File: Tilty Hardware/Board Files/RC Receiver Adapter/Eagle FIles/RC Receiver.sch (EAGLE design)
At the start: 19 parts, among them U1 ATMEGA328P, U2 LM2931, Y1 16MHz

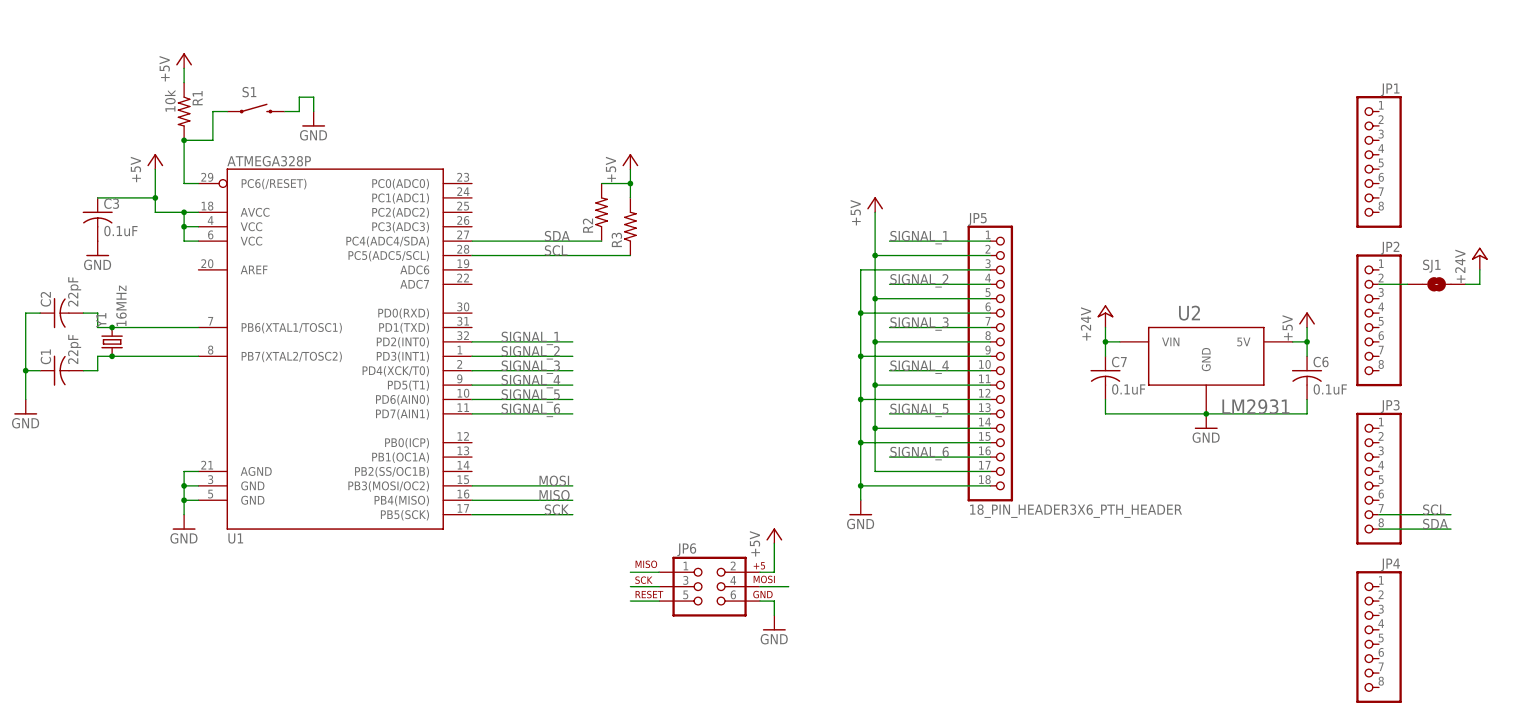
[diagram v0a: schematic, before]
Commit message: Finally got TiltyIMU class working! updated some other programs, worked on RC receiver add-on
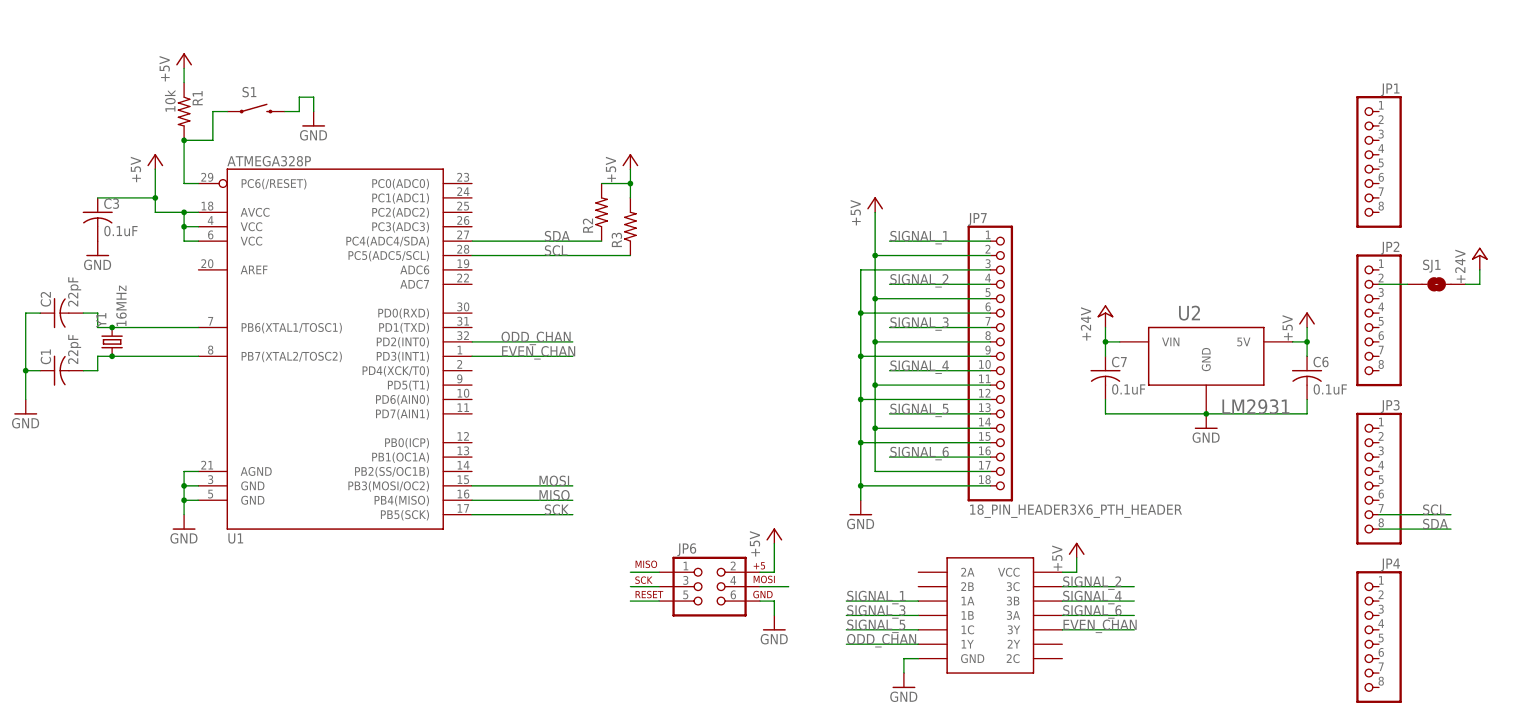
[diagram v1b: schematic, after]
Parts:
- added U$1: C74HC407514-SOIC, My Parts:C74HC407514-SOIC
- Y1: device SparkFun-FreqCtrl:CRYSTALSMD -> SparkFun-FreqCtrl:CRYSTAL5X3
- renumbered JP5 to JP7
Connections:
- new net EVEN_CHAN: U$1.3Y, U1.PD3(INT1)
- new net ODD_CHAN: U$1.1Y, U1.PD2(INT0)
- net +5V: now also U$1.VCC
- net GND: now also U$1.GND
- net SIGNAL_1: now also U$1.1A; no longer U1.PD2(INT0)
- net SIGNAL_2: now also U$1.3C; no longer U1.PD3(INT1)
- net SIGNAL_3: now also U$1.1B; no longer U1.PD4(XCK/T0)
- net SIGNAL_4: now also U$1.3B; no longer U1.PD5(T1)
- net SIGNAL_5: now also U$1.1C; no longer U1.PD6(AIN0)
- net SIGNAL_6: now also U$1.3A; no longer U1.PD7(AIN1)

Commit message: Nearly finished R/C receiver add-on, updated things to-do
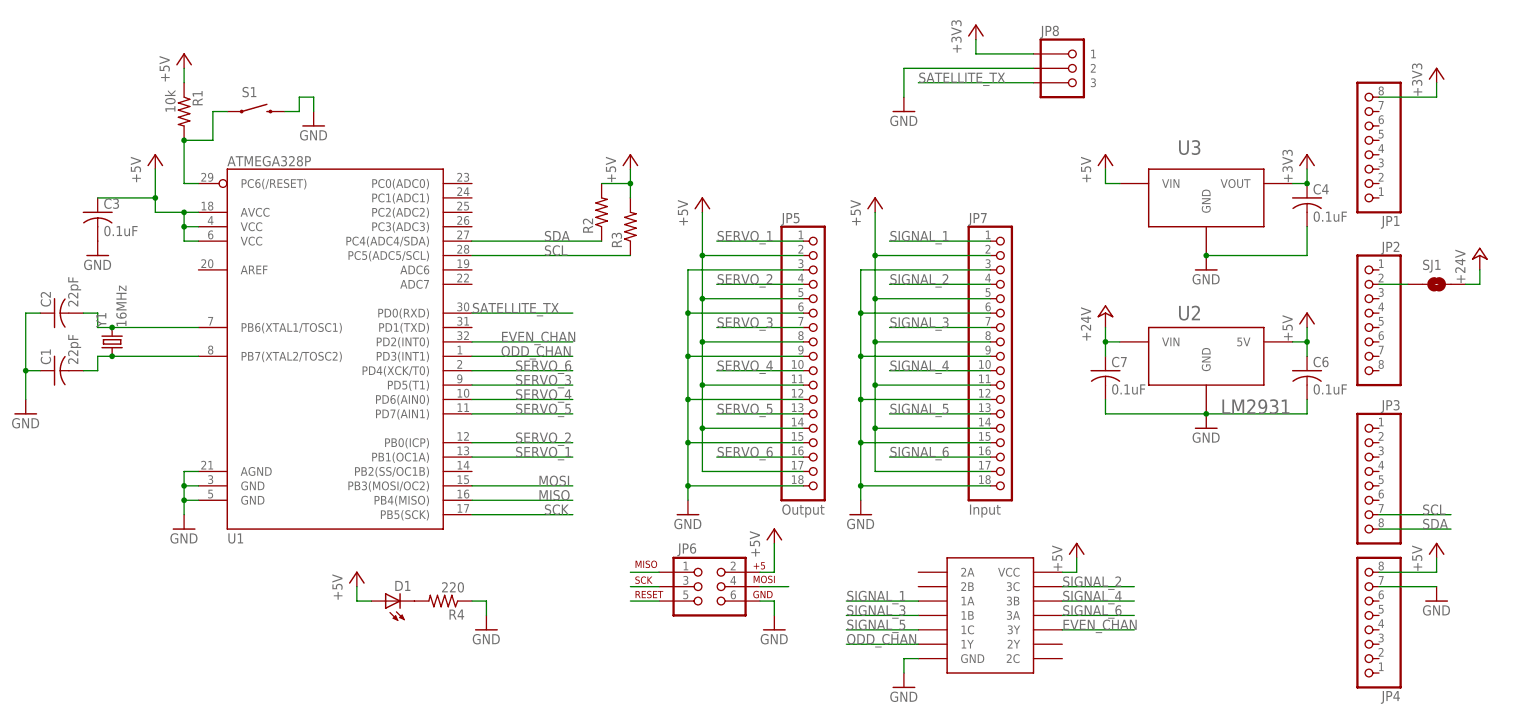
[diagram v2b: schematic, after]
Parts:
- added C4: 0.1uF, resistor:C-USC0603
- added D1: (no value), SparkFun-LED:LED-GREENLED-0805_NO_SILK
- added JP5: Output, My Parts:18_PIN_HEADER3X6_PTH_HEADER
- added JP8: 3-PIN_JST_ZH_PTH_CONNECTORRIGHT_ANGLE_PTH, My Parts:3-PIN_JST_ZH_PTH_CONNECTORRIGHT_ANGLE_PTH
- added R4: 220, resistor:R-US_R0603
- added U3: AP7313SOT23R, My Parts:AP7313SOT23R
- JP7: value 18_PIN_HEADER3X6_PTH_HEADER -> Input
- renumbered U$1 to U4
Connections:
- new net +3V3: C4.1, JP1.8, JP8.1, U3.VOUT
- new net N$8: D1.C, R4.2
- new net SATELLITE_TX: JP8.3, U1.PD0(RXD)
- new net SERVO_1: JP5.1, U1.PB1(OC1A)
- new net SERVO_2: JP5.4, U1.PB0(ICP)
- new net SERVO_3: JP5.7, U1.PD5(T1)
- new net SERVO_4: JP5.10, U1.PD6(AIN0)
- new net SERVO_5: JP5.13, U1.PD7(AIN1)
- new net SERVO_6: JP5.16, U1.PD4(XCK/T0)
- net +5V: now also D1.A, JP4.8, JP5.11, JP5.14, JP5.17, JP5.2, JP5.5, JP5.8, U3.VIN
- net EVEN_CHAN: now also U1.PD2(INT0); no longer U1.PD3(INT1)
- net GND: now also C4.2, JP4.7, JP5.12, JP5.15, JP5.18, JP5.3, JP5.6, JP5.9, JP8.2, R4.1, U3.GND
- net ODD_CHAN: now also U1.PD3(INT1); no longer U1.PD2(INT0)
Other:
- moved on the sheet: JP1, JP4

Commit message: Nearly finished RC Receiver add-on prototype, worked on TiltyIMU library
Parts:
- added JP10: (no value), SparkFun-Connectors:M03X2NO_SILK
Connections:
- new net A0: JP10.1, U1.PC0(ADC0)
- new net A1: JP10.3, U1.PC1(ADC1)
- new net A2: JP10.5, U1.PC2(ADC2)
- new net A3: JP10.6, U1.PC3(ADC3)
- new net ARDUINO_TX: JP10.2, U1.PD1(TXD)
- net GND: now also JP2.1, JP3.1
- net SATELLITE_TX: now also JP10.4
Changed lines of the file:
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@@
 <part name="GND4" library="supply1" deviceset="GND" device=""/>
 <part name="P+4" library="supply1" deviceset="+5V" device=""/>
-<part name="S1" library="SparkFun-Electromechanical" deviceset="SWITCH-MOMENTARY-2" device="SMD"/>
 <part name="GND5" library="supply1" deviceset="GND" device=""/>
 <part name="JP6" library="SparkFun-Connectors" deviceset="AVR_SPI_PRG_6" device="2X3_LOCK"/>
@@
 <part name="R4" library="resistor" deviceset="R-US_" device="R0603" value="220"/>
 <part name="GND13" library="supply1" deviceset="GND" device=""/>
+<part name="GND14" library="supply1" deviceset="GND" device=""/>
+<part name="GND15" library="supply1" deviceset="GND" device=""/>
+<part name="JP10" library="SparkFun-Connectors" deviceset="M03X2" device="NO_SILK"/>
+<part name="S1" library="SparkFun-Electromechanical" deviceset="SWITCH-MOMENTARY-2" device="SMD"/>
 </parts>
 <sheets>
@@
 <instance part="GND4" gate="1" x="35.56" y="40.64"/>
 <instance part="P+4" gate="1" x="30.48" y="106.68"/>
-<instance part="S1" gate="G$1" x="48.26" y="114.3" smashed="yes">
-<attribute name="NAME" x="45.72" y="116.84" size="1.778" layer="95"/>
-</instance>
 <instance part="GND5" gate="1" x="58.42" y="111.76"/>
 <instance part="JP6" gate="G$1" x="127" y="30.48" smashed="yes">
@@
 <instance part="R4" gate="G$1" x="81.28" y="27.94" rot="R180"/>
 <instance part="GND13" gate="1" x="88.9" y="22.86"/>
+<instance part="GND14" gate="1" x="269.24" y="86.36"/>
+<instance part="GND15" gate="1" x="254" y="53.34"/>
+<instance part="JP10" gate="G$1" x="99.06" y="121.92"/>
+<instance part="S1" gate="G$1" x="48.26" y="114.3" smashed="yes">
+<attribute name="NAME" x="45.72" y="116.84" size="1.778" layer="95"/>
+</instance>
 </instances>
 <busses>
@@
 </segment>
 <segment>
-<pinref part="S1" gate="G$1" pin="2"/>
-<wire x1="53.34" y1="114.3" x2="55.88" y2="114.3" width="0.1524" layer="91"/>
 <wire x1="55.88" y1="114.3" x2="55.88" y2="116.84" width="0.1524" layer="91"/>
 <wire x1="55.88" y1="116.84" x2="58.42" y2="116.84" width="0.1524" layer="91"/>
 <pinref part="GND5" gate="1" pin="GND"/>
 <wire x1="58.42" y1="116.84" x2="58.42" y2="114.3" width="0.1524" layer="91"/>
+<pinref part="S1" gate="G$1" pin="2"/>
+<wire x1="55.88" y1="114.3" x2="53.34" y2="114.3" width="0.1524" layer="91"/>
 </segment>
 <segment>
@@
 <wire x1="88.9" y1="27.94" x2="88.9" y2="25.4" width="0.1524" layer="91"/>
 </segment>
+<segment>
+<pinref part="JP2" gate="A" pin="1"/>
+<wire x1="246.38" y1="86.36" x2="251.46" y2="86.36" width="0.1524" layer="91"/>
+<wire x1="251.46" y1="86.36" x2="251.46" y2="93.98" width="0.1524" layer="91"/>
+<wire x1="251.46" y1="93.98" x2="269.24" y2="93.98" width="0.1524" layer="91"/>
+<wire x1="269.24" y1="93.98" x2="269.24" y2="88.9" width="0.1524" layer="91"/>
+<pinref part="GND14" gate="1" pin="GND"/>
+</segment>
+<segment>
+<pinref part="JP3" gate="A" pin="1"/>
+<wire x1="246.38" y1="58.42" x2="254" y2="58.42" width="0.1524" layer="91"/>
+<wire x1="254" y1="58.42" x2="254" y2="55.88" width="0.1524" layer="91"/>
+<pinref part="GND15" gate="1" pin="GND"/>
+</segment>
 </net>
 <net name="+24V" class="0">
@@
 <wire x1="35.56" y1="109.22" x2="35.56" y2="101.6" width="0.1524" layer="91"/>
 <wire x1="35.56" y1="101.6" x2="38.1" y2="101.6" width="0.1524" layer="91"/>
-<pinref part="S1" gate="G$1" pin="1"/>
-<wire x1="43.18" y1="114.3" x2="40.64" y2="114.3" width="0.1524" layer="91"/>
 <wire x1="40.64" y1="114.3" x2="40.64" y2="109.22" width="0.1524" layer="91"/>
 <wire x1="40.64" y1="109.22" x2="35.56" y2="109.22" width="0.1524" layer="91"/>
 <junction x="35.56" y="109.22"/>
+<pinref part="S1" gate="G$1" pin="1"/>
+<wire x1="40.64" y1="114.3" x2="43.18" y2="114.3" width="0.1524" layer="91"/>
 </segment>
 </net>
@@
 <wire x1="86.36" y1="78.74" x2="104.14" y2="78.74" width="0.1524" layer="91"/>
 <label x="86.36" y="78.74" size="1.778" layer="95"/>
+</segment>
+<segment>
+<pinref part="JP10" gate="G$1" pin="4"/>
+<wire x1="106.68" y1="121.92" x2="121.92" y2="121.92" width="0.1524" layer="91"/>
+<label x="106.68" y="121.92" size="1.778" layer="95"/>
 </segment>
 </net>
@@
 </segment>
 </net>
+<net name="ARDUINO_TX" class="0">
+<segment>
+<pinref part="U1" gate="G$1" pin="PD1(TXD)"/>
+<wire x1="86.36" y1="76.2" x2="104.14" y2="76.2" width="0.1524" layer="91"/>
+<label x="88.9" y="76.2" size="1.778" layer="95"/>
+</segment>
+<segment>
+<pinref part="JP10" gate="G$1" pin="2"/>
+<wire x1="106.68" y1="124.46" x2="121.92" y2="124.46" width="0.1524" layer="91"/>
+<label x="106.68" y="124.46" size="1.778" layer="95"/>
+</segment>
+</net>
+<net name="A3" class="0">
+<segment>
+<pinref part="U1" gate="G$1" pin="PC3(ADC3)"/>
+<wire x1="86.36" y1="93.98" x2="91.44" y2="93.98" width="0.1524" layer="91"/>
+<label x="88.9" y="93.98" size="1.778" layer="95"/>
+</segment>
+<segment>
+<pinref part="JP10" gate="G$1" pin="6"/>
+<wire x1="106.68" y1="119.38" x2="121.92" y2="119.38" width="0.1524" layer="91"/>
+<label x="119.38" y="119.38" size="1.778" layer="95"/>
+</segment>
+</net>
+<net name="A1" class="0">
+<segment>
+<wire x1="91.44" y1="121.92" x2="88.9" y2="121.92" width="0.1524" layer="91"/>
+<label x="88.9" y="121.92" size="1.778" layer="95"/>
+<pinref part="JP10" gate="G$1" pin="3"/>
+</segment>
+<segment>
+<pinref part="U1" gate="G$1" pin="PC1(ADC1)"/>
+<wire x1="86.36" y1="99.06" x2="91.44" y2="99.06" width="0.1524" layer="91"/>
+<label x="88.9" y="99.06" size="1.778" layer="95"/>
+</segment>
+</net>
+<net name="A0" class="0">
+<segment>
+<pinref part="U1" gate="G$1" pin="PC0(ADC0)"/>
+<wire x1="86.36" y1="101.6" x2="91.44" y2="101.6" width="0.1524" layer="91"/>
+<label x="88.9" y="101.6" size="1.778" layer="95"/>
+</segment>
+<segment>
+<wire x1="91.44" y1="124.46" x2="88.9" y2="124.46" width="0.1524" layer="91"/>
+<pinref part="JP10" gate="G$1" pin="1"/>
+<label x="88.9" y="124.46" size="1.778" layer="95"/>
+</segment>
+</net>
+<net name="A2" class="0">
+<segment>
+<pinref part="U1" gate="G$1" pin="PC2(ADC2)"/>
+<wire x1="86.36" y1="96.52" x2="91.44" y2="96.52" width="0.1524" layer="91"/>
+<label x="88.9" y="96.52" size="1.778" layer="95"/>
+</segment>
+<segment>
+<wire x1="91.44" y1="119.38" x2="88.9" y2="119.38" width="0.1524" layer="91"/>
+<pinref part="JP10" gate="G$1" pin="5"/>
+<label x="88.9" y="119.38" size="1.778" layer="95"/>
+</segment>
+</net>

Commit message: Updated things.todo and RC Receiver add-on has been ordered
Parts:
- Y1: PART# 535-10226-1-ND -> 887-1104-1-ND
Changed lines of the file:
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@@
 <part name="GND1" library="supply1" deviceset="GND" device=""/>
 <part name="Y1" library="SparkFun-FreqCtrl" deviceset="CRYSTAL" device="5X3" value="16MHz">
-<attribute name="PART#" value="535-10226-1-ND"/>
+<attribute name="PART#" value="887-1104-1-ND"/>
 </part>
 <part name="C1" library="resistor" deviceset="C-US" device="C0603" value="22pF"/>

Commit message: Changed a filter cap value, Lots of bluetooth library work
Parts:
- C6: value 0.1uF -> 4.7uF
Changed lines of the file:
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@@
 <part name="GND9" library="supply1" deviceset="GND" device=""/>
 <part name="P+12" library="supply1" deviceset="+5V" device=""/>
-<part name="C6" library="resistor" deviceset="C-US" device="C0603" value="0.1uF"/>
+<part name="C6" library="resistor" deviceset="C-US" device="C0603" value="4.7uF"/>
 <part name="C7" library="resistor" deviceset="C-US" device="C0603" value="0.1uF"/>
 <part name="P+13" library="supply1" deviceset="+24V" device=""/>
